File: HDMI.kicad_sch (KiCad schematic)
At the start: 6 parts, among them J501 690-019-298-412, U403 TPD4EUSB30, U404 TPD4EUSB30, U501 RT9742SNGV

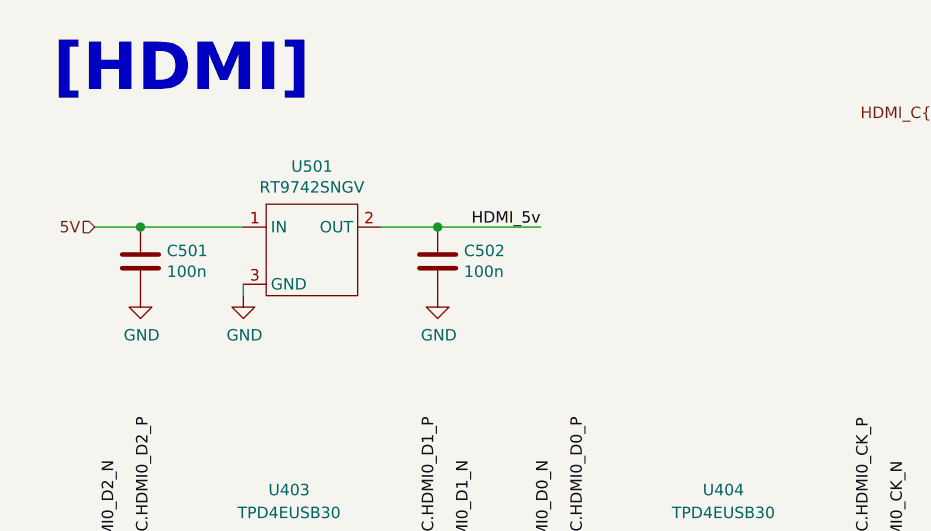
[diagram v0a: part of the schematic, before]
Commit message: changed switch on HDMI
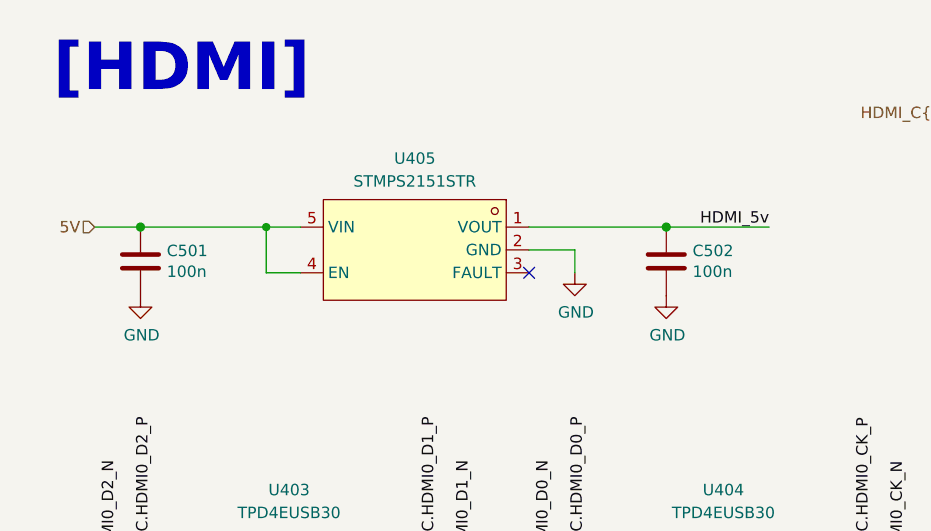
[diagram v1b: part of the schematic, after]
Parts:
- removed U501: RT9742SNGV, Package_TO_SOT_SMD:TSOT-23, symbol CM5IO:RT9742SNGV
- added U405: STMPS2151STR, Package_TO_SOT_SMD:SOT-23-5, symbol EasyEDA:STMPS2151STR
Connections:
- net 5V: now also U405.4 (EN), U405.5 (VIN)
- net GND: now also U405.2 (GND)
- net HDMI_5v: now also U405.1 (VOUT)
- no-connect marks 1 -> 2
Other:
- moved on the sheet: C502
